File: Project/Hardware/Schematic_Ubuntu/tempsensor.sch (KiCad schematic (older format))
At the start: 12 parts, among them U5 MAX4460ESA+

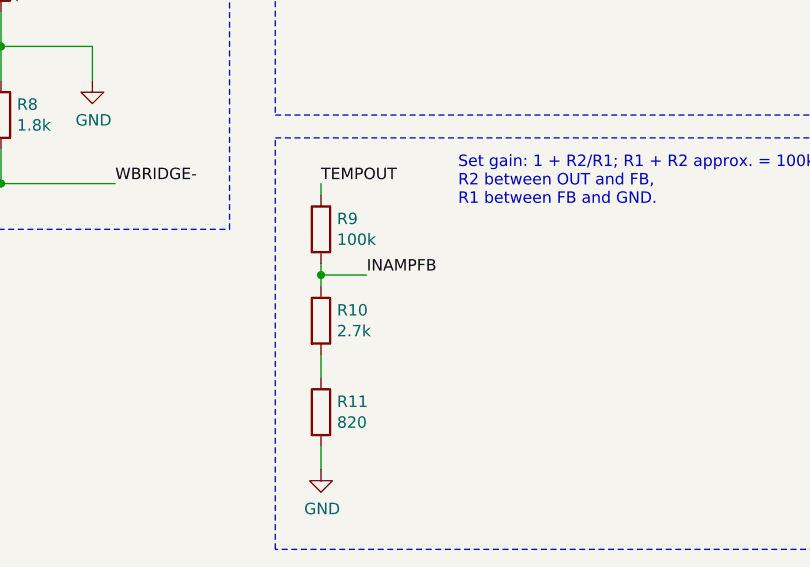
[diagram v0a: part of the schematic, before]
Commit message: Extra resistor till temp gain, två cubemx project med olika pinsmaps, Gerber filer till pcb_revS
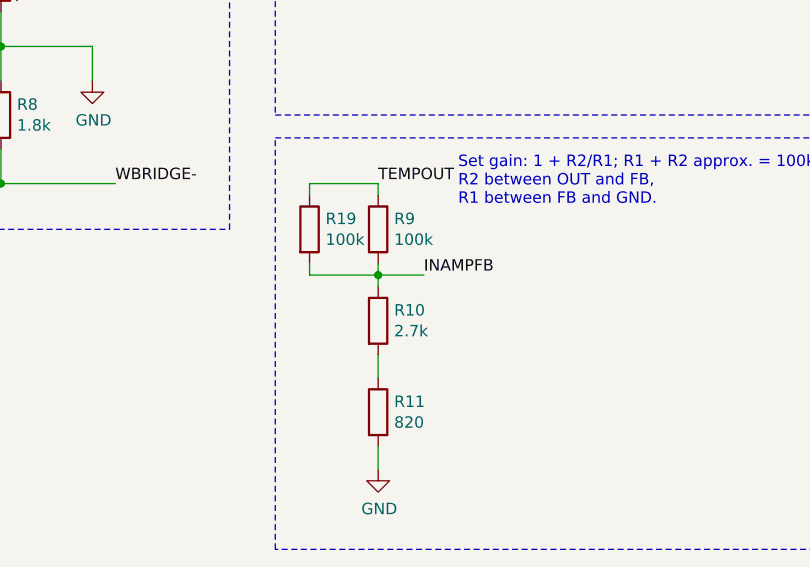
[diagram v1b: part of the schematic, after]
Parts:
- added R19: 100k, Resistors_SMD:R_0805_HandSoldering, symbol Device:R
- U5: footprint TO_SOT_Packages_SMD:SOT-23-8_Handsoldering -> Housings_SOIC:SO-8_5.3x6.2mm_Pitch1.27mm
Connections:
- net INAMPFB: now also R19.2
- net TEMPOUT: now also R19.1
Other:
- moved on the sheet: R10, R11, R9
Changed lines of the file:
@@
 F 0 "U5" H 5600 1887 60  0000 C CNN
 F 1 "MAX4460ESA+" H 5600 1781 60  0000 C CNN
-F 2 "TO_SOT_Packages_SMD:SOT-23-8_Handsoldering" H 5600 1740 60  0001 C CNN
+F 2 "Housings_SOIC:SO-8_5.3x6.2mm_Pitch1.27mm" H 5600 1740 60  0001 C CNN
 F 3 "" H 4500 1500 60  0000 C CNN
 	1    4500 1500
@@
 L Device:R R9
 U 1 1 5C5639FE
-P 4100 3100
-F 0 "R9" H 4170 3146 50  0000 L CNN
-F 1 "100k" H 4170 3055 50  0000 L CNN
-F 2 "Resistors_SMD:R_0805_HandSoldering" V 4030 3100 50  0001 C CNN
-F 3 "~" H 4100 3100 50  0001 C CNN
-	1    4100 3100
+P 4350 3100
+F 0 "R9" H 4420 3146 50  0000 L CNN
+F 1 "100k" H 4420 3055 50  0000 L CNN
+F 2 "Resistors_SMD:R_0805_HandSoldering" V 4280 3100 50  0001 C CNN
+F 3 "~" H 4350 3100 50  0001 C CNN
+	1    4350 3100
 	1    0    0    -1
 $EndComp
@@
 L Device:R R10
 U 1 1 5C563A36
-P 4100 3500
-F 0 "R10" H 4170 3546 50  0000 L CNN
-F 1 "2.7k" H 4170 3455 50  0000 L CNN
-F 2 "Resistors_SMD:R_0805_HandSoldering" V 4030 3500 50  0001 C CNN
-F 3 "~" H 4100 3500 50  0001 C CNN
-	1    4100 3500
-	1    0    0    -1
-$EndComp
-Wire Wire Line
-	4100 2950 4100 2900
-Wire Wire Line
-	4100 3250 4100 3300
-Wire Wire Line
-	4100 3300 4300 3300
-Connection ~ 4100 3300
-Wire Wire Line
-	4100 3300 4100 3350
-Text Label 4300 3300 0    50   ~ 0
+P 4350 3500
+F 0 "R10" H 4420 3546 50  0000 L CNN
+F 1 "2.7k" H 4420 3455 50  0000 L CNN
+F 2 "Resistors_SMD:R_0805_HandSoldering" V 4280 3500 50  0001 C CNN
+F 3 "~" H 4350 3500 50  0001 C CNN
+	1    4350 3500
+	1    0    0    -1
+$EndComp
+Wire Wire Line
+	4350 2950 4350 2900
+Wire Wire Line
+	4350 3250 4350 3300
+Wire Wire Line
+	4350 3300 4550 3300
+Connection ~ 4350 3300
+Wire Wire Line
+	4350 3300 4350 3350
+Text Label 4550 3300 0    50   ~ 0
 INAMPFB
-Text Label 4100 2900 0    50   ~ 0
+Text Label 4350 2900 0    50   ~ 0
 TEMPOUT
 $Comp
 L power:GND #PWR0130
 U 1 1 5C5640C7
-P 4100 4150
-F 0 "#PWR0130" H 4100 3900 50  0001 C CNN
-F 1 "GND" H 4105 3977 50  0000 C CNN
-F 2 "" H 4100 4150 50  0001 C CNN
-F 3 "" H 4100 4150 50  0001 C CNN
-	1    4100 4150
+P 4350 4150
+F 0 "#PWR0130" H 4350 3900 50  0001 C CNN
+F 1 "GND" H 4355 3977 50  0000 C CNN
+F 2 "" H 4350 4150 50  0001 C CNN
+F 3 "" H 4350 4150 50  0001 C CNN
+	1    4350 4150
 	1    0    0    -1
 $EndComp
@@
 L Device:R R11
 U 1 1 5C58C2D0
-P 4100 3900
-F 0 "R11" H 4170 3946 50  0000 L CNN
-F 1 "820" H 4170 3855 50  0000 L CNN
-F 2 "Resistors_SMD:R_0805_HandSoldering" V 4030 3900 50  0001 C CNN
-F 3 "~" H 4100 3900 50  0001 C CNN
-	1    4100 3900
-	1    0    0    -1
-$EndComp
-Wire Wire Line
-	4100 3750 4100 3650
-Wire Wire Line
-	4100 4050 4100 4150
+P 4350 3900
+F 0 "R11" H 4420 3946 50  0000 L CNN
+F 1 "820" H 4420 3855 50  0000 L CNN
+F 2 "Resistors_SMD:R_0805_HandSoldering" V 4280 3900 50  0001 C CNN
+F 3 "~" H 4350 3900 50  0001 C CNN
+	1    4350 3900
+	1    0    0    -1
+$EndComp
+Wire Wire Line
+	4350 4050 4350 4150
 Wire Wire Line
 	1800 2900 1800 2750
@@
 Text HLabel 4500 1500 0    50   Input ~ 0
 TEMPOUT
+$Comp
+L Device:R R19
+U 1 1 5C684C46
+P 4050 3100
+F 0 "R19" H 4120 3146 50  0000 L CNN
+F 1 "100k" H 4120 3055 50  0000 L CNN
+F 2 "Resistors_SMD:R_0805_HandSoldering" V 3980 3100 50  0001 C CNN
+F 3 "~" H 4050 3100 50  0001 C CNN
+	1    4050 3100
+	1    0    0    -1
+$EndComp
+Wire Wire Line
+	4050 3250 4050 3300
+Wire Wire Line
+	4050 3300 4350 3300
+Wire Wire Line
+	4050 2950 4050 2900
+Wire Wire Line
+	4050 2900 4350 2900
+Wire Wire Line
+	4350 3650 4350 3750
 $EndSCHEMATC
